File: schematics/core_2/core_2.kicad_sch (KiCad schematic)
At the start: 35 parts, among them U1 74LS04, U2 74LS574, U3 74LS02, U5 74LS00

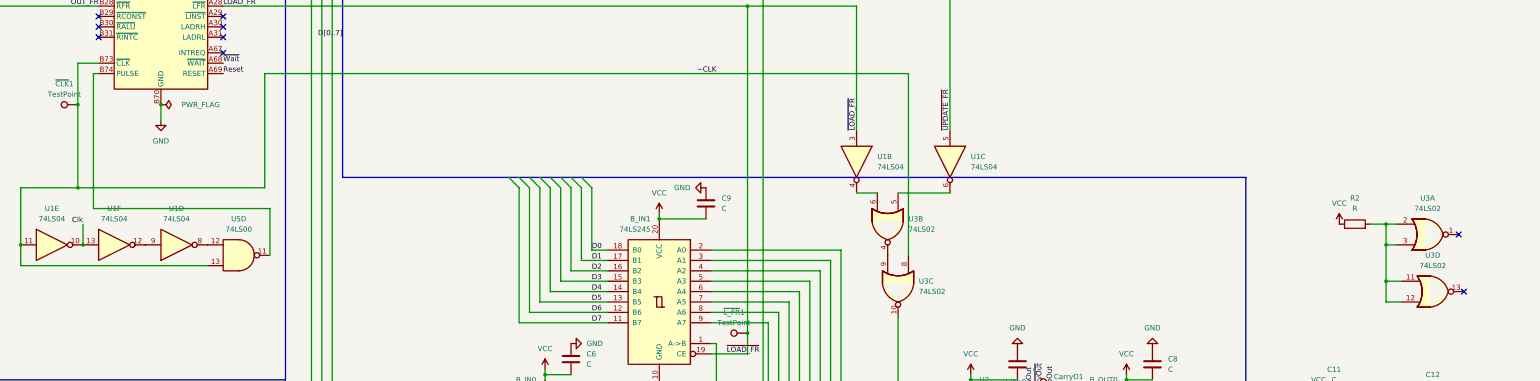
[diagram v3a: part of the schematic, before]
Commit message: Fix inverted pulse
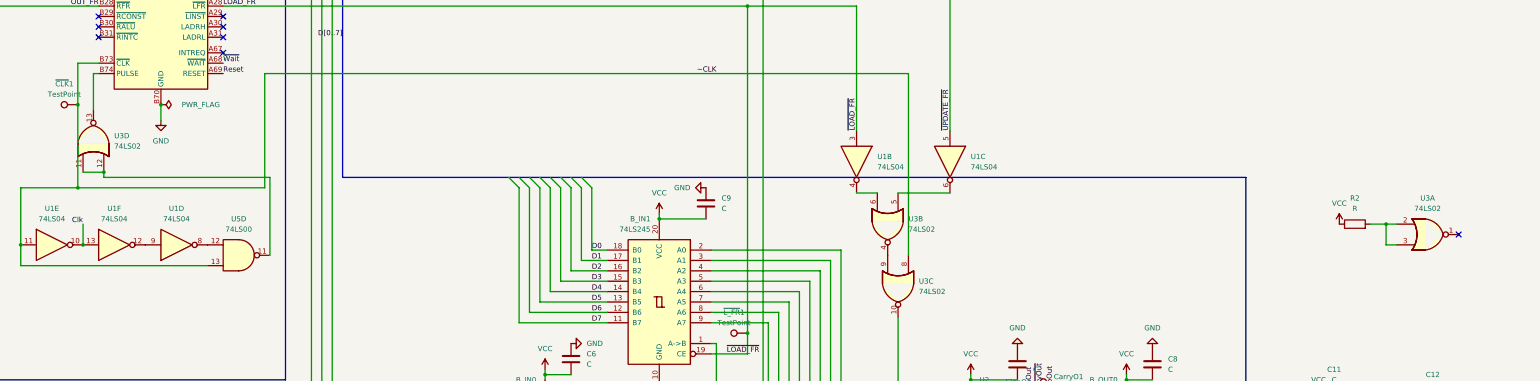
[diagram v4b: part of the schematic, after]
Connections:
- net at R2.2, U3.2, U3.3: no longer U3.11, U3.12
- net at U5.11: now also U3.11, U3.12; no longer BC1.B74 (PULSE)
- net at U3.13: now also BC1.B74 (PULSE)
- no-connect marks 65 -> 64
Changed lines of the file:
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@@
 	)
 	(junction
-		(at 515.62 240.03)
-		(diameter 0)
-		(color 0 0 0 0)
-	)
-	(junction
 		(at 300.99 128.27)
 		(diameter 0)
@@
 	)
 	(junction
+		(at 201.93 213.36)
+		(diameter 0)
+		(color 0 0 0 0)
+	)
+	(junction
 		(at 309.88 304.8)
 		(diameter 0)
@@
 	)
 	(junction
-		(at 515.62 231.14)
-		(diameter 0)
-		(color 0 0 0 0)
-	)
-	(junction
 		(at 363.22 45.72)
 		(diameter 0)
@@
 	)
 	(no_connect
-		(at 534.67 242.57)
-	)
-	(no_connect
 		(at 231.14 162.56)
 	)
@@
 	(wire
 		(pts
-			(xy 199.39 222.25) (xy 199.39 189.23)
-		)
-		(stroke
-			(width 0)
-			(type default)
-		)
-	)
-	(wire
-		(pts
 			(xy 248.92 125.73) (xy 274.32 125.73)
 		)
@@
 	(wire
 		(pts
-			(xy 515.62 245.11) (xy 519.43 245.11)
-		)
-		(stroke
-			(width 0)
-			(type default)
-		)
-	)
-	(wire
-		(pts
 			(xy 299.72 125.73) (xy 300.99 125.73)
 		)
@@
 	(wire
 		(pts
-			(xy 515.62 240.03) (xy 519.43 240.03)
+			(xy 242.57 214.63) (xy 201.93 214.63)
 		)
 		(stroke
@@
 	(wire
 		(pts
-			(xy 97.79 137.16) (xy 105.41 137.16)
+			(xy 196.85 213.36) (xy 201.93 213.36)
 		)
 		(stroke
@@
 	(wire
 		(pts
-			(xy 350.52 232.41) (xy 382.27 232.41)
+			(xy 97.79 137.16) (xy 105.41 137.16)
 		)
 		(stroke
@@
 	(wire
 		(pts
-			(xy 97.79 241.3) (xy 105.41 241.3)
+			(xy 350.52 232.41) (xy 382.27 232.41)
 		)
 		(stroke
@@
 	(wire
 		(pts
-			(xy 379.73 274.32) (xy 401.32 274.32)
+			(xy 97.79 241.3) (xy 105.41 241.3)
 		)
 		(stroke
@@
 	(wire
 		(pts
-			(xy 242.57 222.25) (xy 199.39 222.25)
+			(xy 379.73 274.32) (xy 401.32 274.32)
 		)
 		(stroke
@@
 	(wire
 		(pts
-			(xy 242.57 233.68) (xy 242.57 222.25)
+			(xy 242.57 214.63) (xy 242.57 233.68)
 		)
 		(stroke
@@
 	(wire
 		(pts
-			(xy 515.62 240.03) (xy 515.62 245.11)
+			(xy 322.58 297.18) (xy 347.98 297.18)
 		)
 		(stroke
 			(width 0)
 			(type default)
+			(color 194 0 0 1)
 		)
 	)
 	(wire
 		(pts
-			(xy 322.58 297.18) (xy 347.98 297.18)
+			(xy 201.93 214.63) (xy 201.93 213.36)
 		)
 		(stroke
 			(width 0)
 			(type default)
-			(color 194 0 0 1)
 		)
 	)
@@
 		)
 	)
-	(wire
-		(pts
-			(xy 515.62 231.14) (xy 515.62 240.03)
-		)
-		(stroke
-			(width 0)
-			(type default)
-		)
-	)
 	(bus
 		(pts
@@
 	(wire
 		(pts
+			(xy 199.39 198.12) (xy 199.39 189.23)
+		)
+		(stroke
+			(width 0)
+			(type default)
+		)
+	)
+	(wire
+		(pts
 			(xy 414.02 262.89) (xy 414.02 264.16)
 		)
@@
 	)
 	(symbol
-		(lib_id "74xx:74LS02")
-		(at 527.05 242.57 0)
-		(unit 4)
-		(exclude_from_sim no)
-		(in_bom yes)
-		(on_board yes)
-		(dnp no)
-		(fields_autoplaced yes)
-		(property "Reference" "U3"
-			(at 527.05 233.68 0)
-			(effects
-				(font
-					(size 1.27 1.27)
-				)
-			)
-		)
-		(property "Value" "74LS02"
-			(at 527.05 236.22 0)
-			(effects
-				(font
-					(size 1.27 1.27)
-				)
-			)
-		)
-		(property "Footprint" "Package_DIP:DIP-14_W7.62mm_Socket_LongPads"
-			(at 527.05 242.57 0)
-			(effects
-				(font
-					(size 1.27 1.27)
-				)
-				(hide yes)
-			)
-		)
-		(property "Datasheet" "http://www.ti.com/lit/gpn/sn74ls02"
-			(at 527.05 242.57 0)
-			(effects
-				(font
-					(size 1.27 1.27)
-				)
-				(hide yes)
-			)
-		)
-		(property "Description" "quad 2-input NOR gate"
-			(at 527.05 242.57 0)
-			(effects
-				(font
-					(size 1.27 1.27)
-				)
-				(hide yes)
-			)
-		)
-		(pin "6"
-		)
-		(pin "1"
-		)
-		(pin "5"
-		)
-		(pin "8"
-		)
-		(pin "9"
-		)
-		(pin "10"
-		)
-		(pin "7"
-		)
-		(pin "12"
-		)
-		(pin "11"
-		)
-		(pin "13"
-		)
-		(pin "3"
-		)
-		(pin "4"
-		)
-		(pin "14"
-		)
-		(pin "2"
-		)
-		(instances
-			(project "core_1"
-				(path "/59b2db81-41fa-4862-96ef-fb4ce3ab7be6"
-					(reference "U3")
-					(unit 4)
-				)
-			)
-		)
-	)
-	(symbol
 		(lib_id "Device:C")
 		(at 219.71 55.88 90)
@@
 				)
 			)
+		)
+	)
+	(symbol
+		(lib_id "74xx:74LS02")
+		(at 199.39 205.74 90)
+		(unit 4)
+		(exclude_from_sim no)
+		(in_bom yes)
+		(on_board yes)
+		(dnp no)
+		(fields_autoplaced yes)
+		(property "Reference" "U3"
+			(at 204.47 204.4699 90)
+			(effects
+				(font
+					(size 1.27 1.27)
+				)
+				(justify right)
+			)
+		)
+		(property "Value" "74LS02"
+			(at 204.47 207.0099 90)
+			(effects
+				(font
+					(size 1.27 1.27)
+				)
+				(justify right)
+			)
+		)
+		(property "Footprint" "Package_DIP:DIP-14_W7.62mm_Socket_LongPads"
+			(at 199.39 205.74 0)
+			(effects
+				(font
+					(size 1.27 1.27)
+				)
+				(hide yes)
+			)
+		)
+		(property "Datasheet" "http://www.ti.com/lit/gpn/sn74ls02"
+			(at 199.39 205.74 0)
+			(effects
+				(font
+					(size 1.27 1.27)
+				)
+				(hide yes)
+			)
+		)
+		(property "Description" "quad 2-input NOR gate"
+			(at 199.39 205.74 0)
+			(effects
+				(font
+					(size 1.27 1.27)
+				)
+				(hide yes)
+			)
+		)
+		(pin "6"
+		)
+		(pin "1"
+		)
+		(pin "5"
+		)
+		(pin "8"
+		)
+		(pin "9"
+		)
+		(pin "10"
+		)
+		(pin "7"
+		)
+		(pin "12"
+		)
+		(pin "11"
+		)
+		(pin "13"
+		)
+		(pin "3"
+		)
+		(pin "4"
+		)
+		(pin "14"
+		)
+		(pin "2"
+		)
+		(instances
+			(project "core_2"
+				(path "/59b2db81-41fa-4862-96ef-fb4ce3ab7be6"
+					(reference "U3")
+					(unit 4)
+				)
+			)

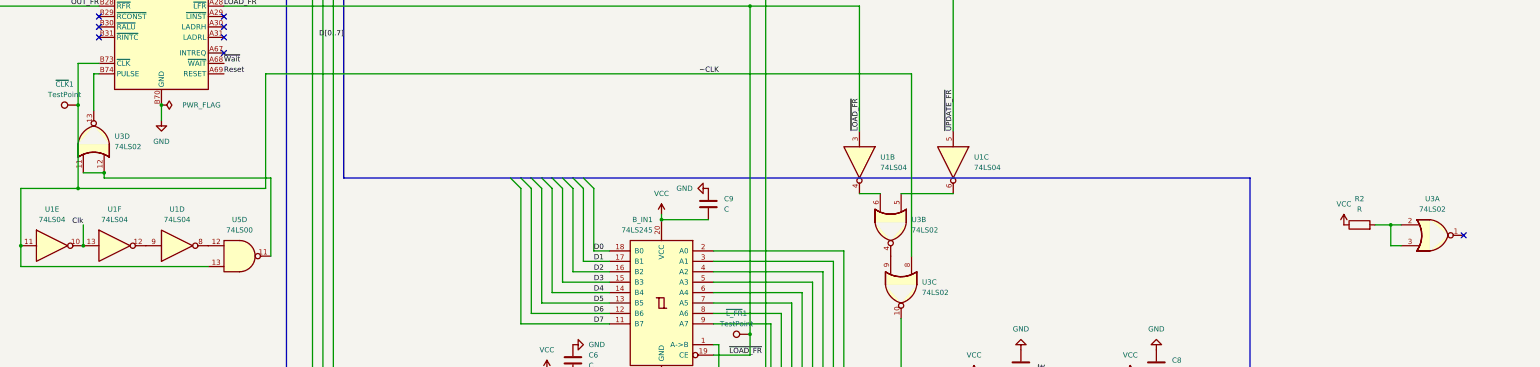
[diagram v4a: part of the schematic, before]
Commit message: Fix pulse detector
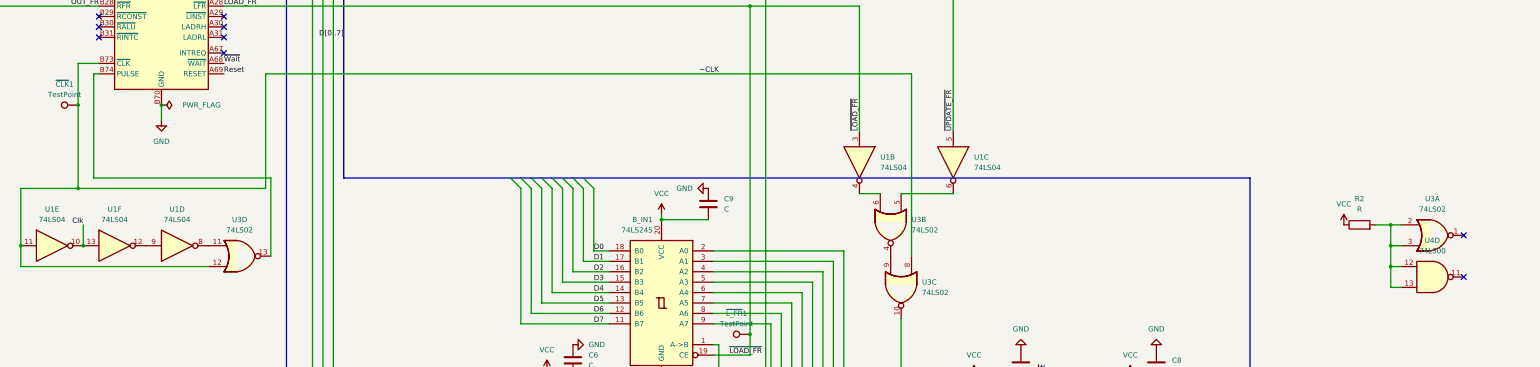
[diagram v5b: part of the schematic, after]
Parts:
- removed unit 4 of U5
- added U4: 74LS00, Package_DIP:DIP-14_W7.62mm_Socket_LongPads, symbol 74xx:74LS00
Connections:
- net ~CLK: now also U3.12
- net at R2.2, U3.2, U3.3: now also U4.12, U4.13
- net at U3.11: now also U1.8; no longer U3.12
- no-connect marks 64 -> 65

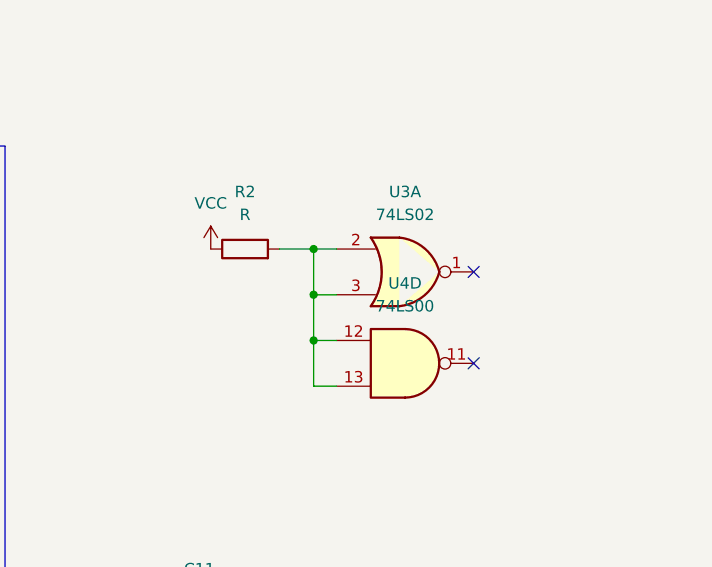
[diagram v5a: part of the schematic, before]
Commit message: Remake with ic74373
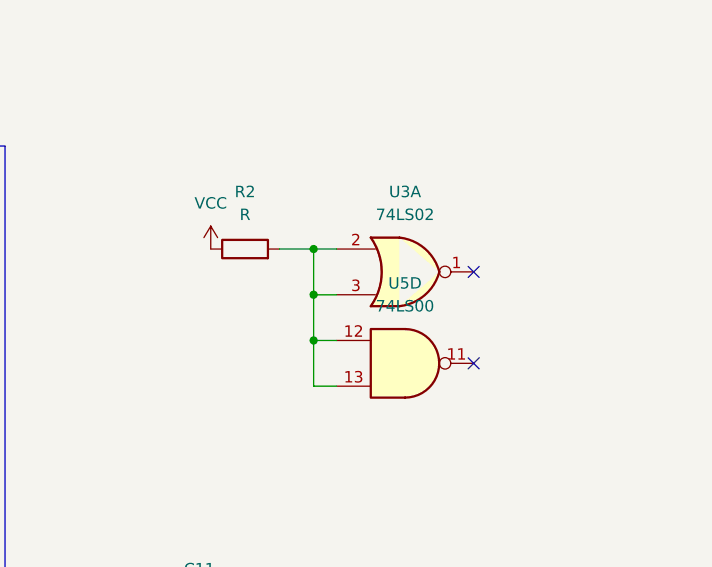
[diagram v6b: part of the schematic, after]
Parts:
- renumbered U4 to U5
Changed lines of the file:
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@@
 		(dnp no)
 		(fields_autoplaced yes)
-		(property "Reference" "U4"
+		(property "Reference" "U5"
 			(at 525.7717 229.87 0)
 			(effects
@@
 			(project "core_2"
 				(path "/59b2db81-41fa-4862-96ef-fb4ce3ab7be6"
-					(reference "U4")
+					(reference "U5")
 					(unit 4)
 				)
